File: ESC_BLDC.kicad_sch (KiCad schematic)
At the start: 95 parts, among them J1 Conn_01x06_Pin, J2 Conn_01x04_Pin, U4 LM339, U5 AP1509-50SG-13, U6 MCP6002-xP, U7 MCP6002-xP, U8 MCP6002-xP

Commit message: ordenado por funcion
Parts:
- added unit 4 of U4
- DBUCK1: footprint Diode_SMD:D_1206_3216Metric_Pad1.42x1.75mm_HandSolder -> Diode_THT:D_DO-34_SOD68_P7.62mm_Horizontal
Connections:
- no-connect marks 28 -> 31
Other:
- note added: "Para evitar errores en las reglas de diseño"
- moved on the sheet: U4E, U6C, U7C, U8C

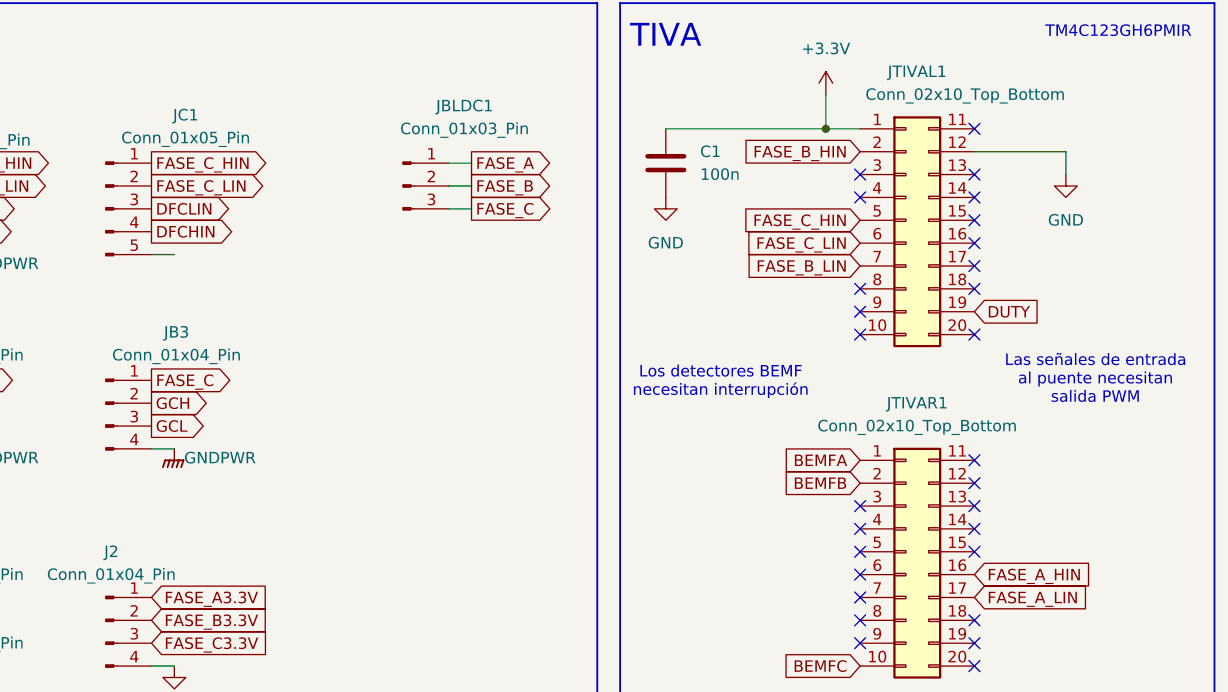
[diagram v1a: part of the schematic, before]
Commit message: Huella de la tiva, conectores SPI
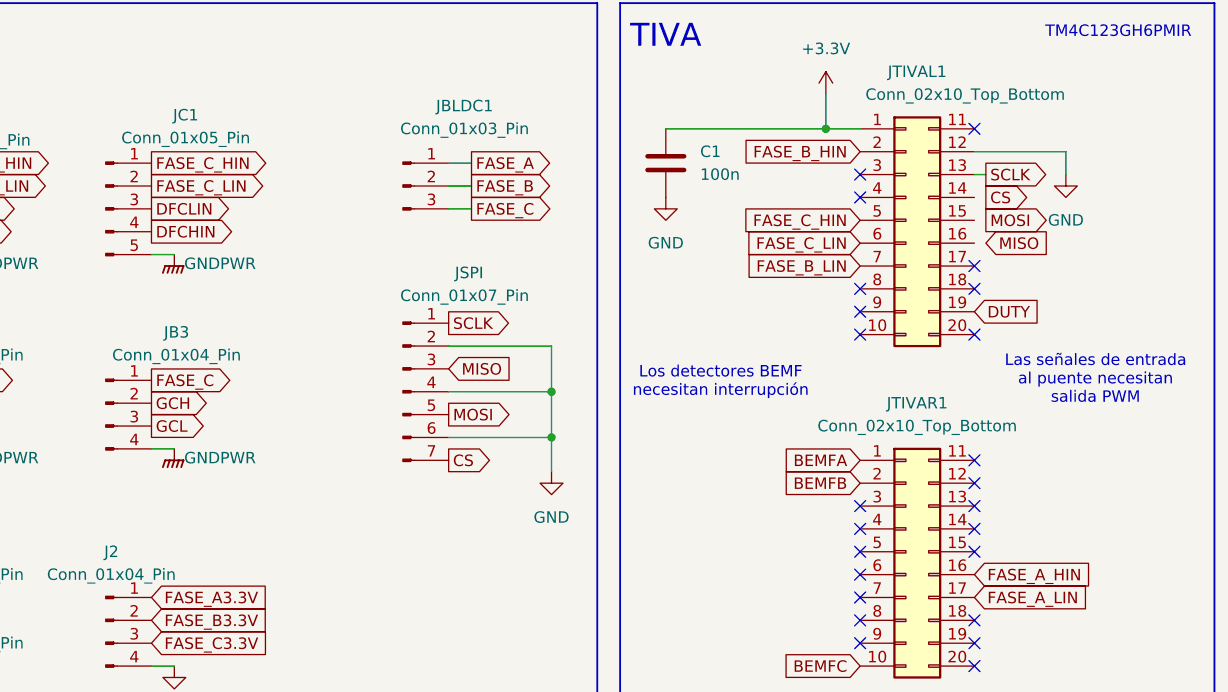
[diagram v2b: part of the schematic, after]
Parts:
- added JSPI: Conn_01x07_Pin, symbol Connector:Conn_01x07_Pin
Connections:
- net GND: now also JSPI.2 (Pin_2), JSPI.4 (Pin_4), JSPI.6 (Pin_6)
- net GNDPWR: now also JC1.5 (Pin_5)
- net SCLK: now reaches JTIVAL1.13 (Pin_13)
- net SCLK: now also JSPI.1 (Pin_1)
- new net CS: JSPI.7 (Pin_7)
- new net MISO: JSPI.3 (Pin_3)
- new net MOSI: JSPI.5 (Pin_5)
- no-connect marks 31 -> 27

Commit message: Colocacion de mosfets y drivers
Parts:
- removed QAH1, QAL1, QBH1, QBL1, QCH1, QCL1: IRLR2905TRPBF, Package_TO_SOT_THT:TO-5-3, symbol JLCImport:IRLR2905TRPBF
- removed U1, U2, U3: ~, Package_DIP:CERDIP-8_W7.62mm_SideBrazed_LongPads_Socket, symbol Driver_FET:IR2301
- added MOSFET1, MOSFET2, MOSFET3, MOSFET4, MOSFET5, MOSFET6: IRFR1205TRPBF, D-PAK_TO-252AA_INF, symbol IRFR1205TRPBF:IRFR1205TRPBF
- added U10, U11, U9: IR2301SPBF, Package_SO:SOIC-8_3.9x4.9mm_P1.27mm, symbol JLCImport:IR2301SPBF
- renumbered JSPI to JSPI1
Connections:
- net DFAHIN: now also U9.2 (HIN)
- net DFALIN: now also U9.3 (LIN)
- net DFBHIN: now also U10.2 (HIN)
- net DFBLIN: now also U10.3 (LIN)
- net DFCHIN: now also U11.2 (HIN)
- net DFCLIN: now also U11.3 (LIN)
- net FASE_A: now also MOSFET5.3 (S), MOSFET6.2 (D), U9.6 (VS)
- net FASE_B: now also MOSFET1.3 (S), MOSFET2.2 (D), U10.6 (VS)
- net FASE_C: now also MOSFET3.3 (S), MOSFET4.2 (D), U11.6 (VS)
- net GAH: now also MOSFET5.1 (G)
- net GAL: now also MOSFET6.1 (G)
- net GBH: now also MOSFET1.1 (G)
- net GBL: now also MOSFET2.1 (G)
- net GCH: now also MOSFET3.1 (G)
- net GCL: now also MOSFET4.1 (G)
- net GNDPWR: now also MOSFET2.3 (S), MOSFET4.3 (S), MOSFET6.3 (S), U10.4 (COM), U11.4 (COM), U9.4 (COM)
- net VBA: now also U9.8 (VB)
- net VBB: now also U10.8 (VB)
- net VBC: now also U11.8 (VB)
- net VCC: now also MOSFET1.2 (D), MOSFET3.2 (D), MOSFET5.2 (D), U10.1 (VCC), U11.1 (VCC), U9.1 (VCC)
- net at RGAL1.2: now also U9.5 (LO)
- net at RGBL1.2: now also U10.5 (LO)
- net at RGBH1.2: now also U10.7 (HO)
- net at RGCL1.2: now also U11.5 (LO)
- net at RGCH1.2: now also U11.7 (HO)
- net at RGAH1.2: now also U9.7 (HO)
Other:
- moved on the sheet: CABO1, CADES1, CBBO1, CBDES1, CCBO1, CCDES1, D2, D3, D4, RGAH1, RGAL1, RGBH1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

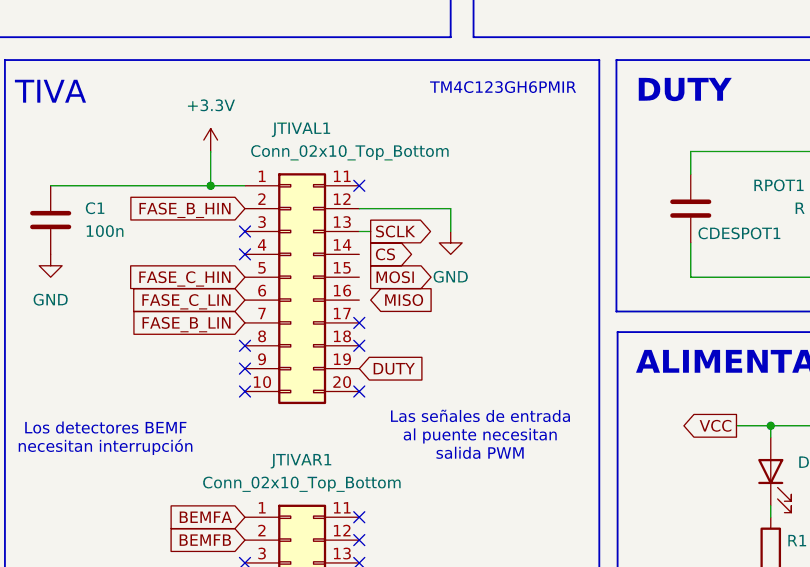
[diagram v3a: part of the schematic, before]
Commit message: Colocacion de dispositivos de potencia
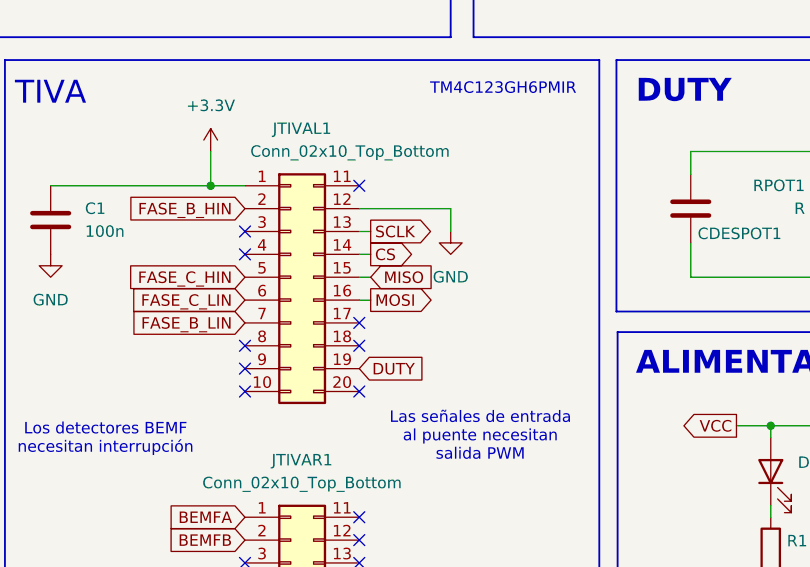
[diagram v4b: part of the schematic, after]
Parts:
- JSPI1: footprint (none) -> Connector_PinHeader_2.54mm:PinHeader_1x07_P2.54mm_Vertical
- MOSFET1, MOSFET2, MOSFET3, MOSFET4, MOSFET5, MOSFET6: footprint D-PAK_TO-252AA_INF -> IRFR1205TRPBF:D-PAK_TO-252AA_INF
- U4: footprint (none) -> Package_SO:SOIC-14_3.9x8.7mm_P1.27mm
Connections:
- net CS: now also JTIVAL1.14 (Pin_14)
- net MISO: now also JTIVAL1.15 (Pin_15)
- net MOSI: now also JTIVAL1.16 (Pin_16)
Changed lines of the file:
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@@
 		)
 	)
+	(wire
+		(pts
+			(xy 165.1 219.71) (xy 166.37 219.71)
+		)
+		(stroke
+			(width 0)
+			(type default)
+		)
+	)
 	(polyline
 		(pts
@@
 		)
 	)
+	(wire
+		(pts
+			(xy 165.1 224.79) (xy 166.37 224.79)
+		)
+		(stroke
+			(width 0)
+			(type default)
+		)
+	)
 	(polyline
 		(pts
@@
 		)
 	)
+	(wire
+		(pts
+			(xy 165.1 222.25) (xy 166.37 222.25)
+		)
+		(stroke
+			(width 0)
+			(type default)
+		)
+	)
 	(polyline
 		(pts
@@
 		)
 	)
+	(global_label "MOSI"
+		(shape output)
+		(at 166.37 224.79 0)
+		(fields_autoplaced yes)
+		(effects
+			(font
+				(size 1.27 1.27)
+			)
+			(justify left)
+		)
+		(property "Intersheetrefs" "${INTERSHEET_REFS}"
+			(at 173.9514 224.79 0)
+			(effects
+				(font
+					(size 1.27 1.27)
+				)
+				(justify left)
+				(hide yes)
+			)
+		)
+	)
 	(global_label "FASE_B3.3V"
 		(shape input)
@@
 		)
 	)
-	(global_label "MISO"
-		(shape input)
-		(at 166.37 224.79 0)
-		(fields_autoplaced yes)
-		(effects
-			(font
-				(size 1.27 1.27)
-			)
-			(justify left)
-		)
-		(property "Intersheetrefs" "${INTERSHEET_REFS}"
-			(at 173.9514 224.79 0)
-			(effects
-				(font
-					(size 1.27 1.27)
-				)
-				(justify left)
-				(hide yes)
-			)
-		)
-	)
 	(global_label "BEMFA"
 		(shape input)
@@
 		)
 	)
+	(global_label "MISO"
+		(shape input)
+		(at 166.37 222.25 0)
+		(fields_autoplaced yes)
+		(effects
+			(font
+				(size 1.27 1.27)
+			)
+			(justify left)
+		)
+		(property "Intersheetrefs" "${INTERSHEET_REFS}"
+			(at 173.9514 222.25 0)
+			(effects
+				(font
+					(size 1.27 1.27)
+				)
+				(justify left)
+				(hide yes)
+			)
+		)
+	)
 	(global_label "DFCHIN"
 		(shape output)
@@
 		)
 	)
-	(global_label "MOSI"
-		(shape output)
-		(at 166.37 222.25 0)
-		(fields_autoplaced yes)
-		(effects
-			(font
-				(size 1.27 1.27)
-			)
-			(justify left)
-		)
-		(property "Intersheetrefs" "${INTERSHEET_REFS}"
-			(at 173.9514 222.25 0)
-			(effects
-				(font
-					(size 1.27 1.27)
-				)
-				(justify left)
-				(hide yes)
-			)
-		)
-	)
 	(netclass_flag ""
 		(length 0.6)
@@
 		(length 0.6)
 		(shape dot)
+		(at 165.1 217.17 0)
+		(fields_autoplaced yes)
+		(effects
+			(font
+				(size 1.27 1.27)
+				(color 24 189 0 1)
+			)
+			(justify left bottom)
+		)
+		(property "Netclass" "Analogico"
+			(at 165.7985 216.57 0)
+			(effects
+				(font
+					(size 1.27 1.27)
+				)
+				(justify left)
+				(hide yes)
+			)
+		)
+		(property "Component Class" ""
+			(at -54.61 182.88 0)
+			(effects
+				(font
+					(size 1.27 1.27)
+					(italic yes)
+				)
+				(hide yes)
+			)
+		)
+	)
+	(netclass_flag ""
+		(length 0.6)
+		(shape dot)
 		(at 40.64 48.26 0)
 		(fields_autoplaced yes)
@@
 		(length 0.6)
 		(shape dot)
+		(at 165.1 219.71 0)
+		(fields_autoplaced yes)
+		(effects
+			(font
+				(size 1.27 1.27)
+				(color 24 189 0 1)
+			)
+			(justify left bottom)
+		)
+		(property "Netclass" "Analogico"
+			(at 165.7985 219.11 0)
+			(effects
+				(font
+					(size 1.27 1.27)
+				)
+				(justify left)
+				(hide yes)
+			)
+		)
+		(property "Component Class" ""
+			(at -54.61 185.42 0)
+			(effects
+				(font
+					(size 1.27 1.27)
+					(italic yes)
+				)
+				(hide yes)
+			)
+		)
+	)
+	(netclass_flag ""
+		(length 0.6)
+		(shape dot)
 		(at 86.36 102.87 0)
 		(fields_autoplaced yes)
@@
 		(length 0.6)
 		(shape dot)
+		(at 165.1 224.79 0)
+		(fields_autoplaced yes)
+		(effects
+			(font
+				(size 1.27 1.27)
+				(color 24 189 0 1)
+			)
+			(justify left bottom)
+		)
+		(property "Netclass" "Analogico"
+			(at 165.7985 224.19 0)
+			(effects
+				(font
+					(size 1.27 1.27)
+				)
+				(justify left)
+				(hide yes)
+			)
+		)
+		(property "Component Class" ""
+			(at -54.61 190.5 0)
+			(effects
+				(font
+					(size 1.27 1.27)
+					(italic yes)
+				)
+				(hide yes)
+			)
+		)
+	)
+	(netclass_flag ""
+		(length 0.6)
+		(shape dot)
 		(at 40.64 163.83 0)
 		(fields_autoplaced yes)
@@
 		(length 0.6)
 		(shape dot)
+		(at 165.1 222.25 0)
+		(fields_autoplaced yes)
+		(effects
+			(font
+				(size 1.27 1.27)
+				(color 24 189 0 1)
+			)
+			(justify left bottom)
+		)
+		(property "Netclass" "Analogico"
+			(at 165.7985 221.65 0)
+			(effects
+				(font
+					(size 1.27 1.27)
+				)
+				(justify left)
+				(hide yes)
+			)
+		)
+		(property "Component Class" ""
+			(at -54.61 187.96 0)
+			(effects
+				(font
+					(size 1.27 1.27)
+					(italic yes)
+				)
+				(hide yes)
+			)
+		)
+	)
+	(netclass_flag ""
+		(length 0.6)
+		(shape dot)
 		(at 127 162.56 0)
 		(fields_autoplaced yes)
@@
 			)
 		)
-		(property "Footprint" ""
+		(property "Footprint" "Connector_PinHeader_2.54mm:PinHeader_1x07_P2.54mm_Vertical"
 			(at 101.6 241.3 0)
 			(effects
@@
 			)
 		)
-		(property "Footprint" "D-PAK_TO-252AA_INF"
+		(property "Footprint" "IRFR1205TRPBF:D-PAK_TO-252AA_INF"
 			(at 87.63 162.56 0)
 			(effects
@@
 			)
 		)
-		(property "Footprint" "D-PAK_TO-252AA_INF"
+		(property "Footprint" "IRFR1205TRPBF:D-PAK_TO-252AA_INF"
 			(at 87.63 53.34 0)
 			(effects
@@
 			)
 		)
-		(property "Footprint" "D-PAK_TO-252AA_INF"
+		(property "Footprint" "IRFR1205TRPBF:D-PAK_TO-252AA_INF"
 			(at 87.63 175.26 0)
 			(effects
@@
 			)
 		)
-		(property "Footprint" "D-PAK_TO-252AA_INF"
+		(property "Footprint" "IRFR1205TRPBF:D-PAK_TO-252AA_INF"
 			(at 87.63 102.87 0)
 			(effects
@@
 			)
 		)
-		(property "Footprint" "D-PAK_TO-252AA_INF"
+		(property "Footprint" "IRFR1205TRPBF:D-PAK_TO-252AA_INF"
 			(at 87.63 40.64 0)
 			(effects
@@
 			)
 		)
-		(property "Footprint" "D-PAK_TO-252AA_INF"
+		(property "Footprint" "IRFR1205TRPBF:D-PAK_TO-252AA_INF"
 			(at 87.63 115.57 0)
 			(effects
@@
 			)
 		)
-		(property "Footprint" ""
+		(property "Footprint" "Package_SO:SOIC-14_3.9x8.7mm_P1.27mm"
 			(at 275.59 118.11 0)
 			(effects

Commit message: Mas colocacion: Testpoints y alguna cosa mas
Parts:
- removed JA1, JB1, JC1: Conn_01x05_Pin, Connector_PinHeader_2.54mm:PinHeader_1x05_P2.54mm_Vertical, symbol Connector:Conn_01x05_Pin
- removed JTIVAL1, JTIVAR1: Conn_02x10_Top_Bottom, Connector_PinHeader_2.54mm:PinHeader_2x10_P2.54mm_Vertical, symbol Connector_Generic:Conn_02x10_Top_Bottom
- added JCONTROL1: Conn_01x07_Pin, Connector_PinSocket_2.54mm:PinSocket_1x07_P2.54mm_Vertical, symbol Connector:Conn_01x07_Pin
- added JTIVAL1, JTIVAR1: Conn_02x10_Odd_Even, Connector_PinHeader_2.54mm:PinHeader_2x10_P2.54mm_Vertical, symbol Connector_Generic:Conn_02x10_Odd_Even
- renumbered JA2 to JA1, JB2 to JB1, J1 to JBEMF1, JB3 to JC1
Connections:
- net +3.3V: now also JTIVAL1.1 (Pin_1)
- net BEMFA: now also JTIVAR1.1 (Pin_1)
- net BEMFB: now also JTIVAR1.3 (Pin_3)
- net BEMFC: now also JTIVAR1.19 (Pin_19)
- net CS: now also JTIVAL1.8 (Pin_8)
- net DUTY: now also JTIVAL1.18 (Pin_18)
- net FASE_A_HIN: now also JCONTROL1.1 (Pin_1), JTIVAR1.12 (Pin_12)
- net FASE_A_LIN: now also JCONTROL1.2 (Pin_2), JTIVAR1.14 (Pin_14)
- net FASE_B_HIN: now also JCONTROL1.3 (Pin_3), JTIVAL1.3 (Pin_3)
- net FASE_B_LIN: now also JCONTROL1.4 (Pin_4), JTIVAL1.13 (Pin_13)
- net FASE_C_HIN: now also JCONTROL1.5 (Pin_5), JTIVAL1.9 (Pin_9)
- net FASE_C_LIN: now also JCONTROL1.6 (Pin_6), JTIVAL1.11 (Pin_11)
- net GND: now also JCONTROL1.7 (Pin_7), JTIVAL1.4 (Pin_4)
- net MISO: now also JTIVAL1.10 (Pin_10)
- net MOSI: now also JTIVAL1.12 (Pin_12)
- net SCLK: now also JTIVAL1.6 (Pin_6)
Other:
- moved on the sheet: JA1, JB1, JC1
